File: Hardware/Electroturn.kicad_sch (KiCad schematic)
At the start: 29 parts, among them J1 Encoder Terminal, J2 Stepper Motor Terminal, SW1 Feed Switch, SW2 Motor Braking Switch, SW3 Mode Right Scroll, SW4 Mode Left Scroll, SW5 Function Btn 1, SW6 Function Btn 2, SW7 Function Btn 2, SW8 Control Panel Encoder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

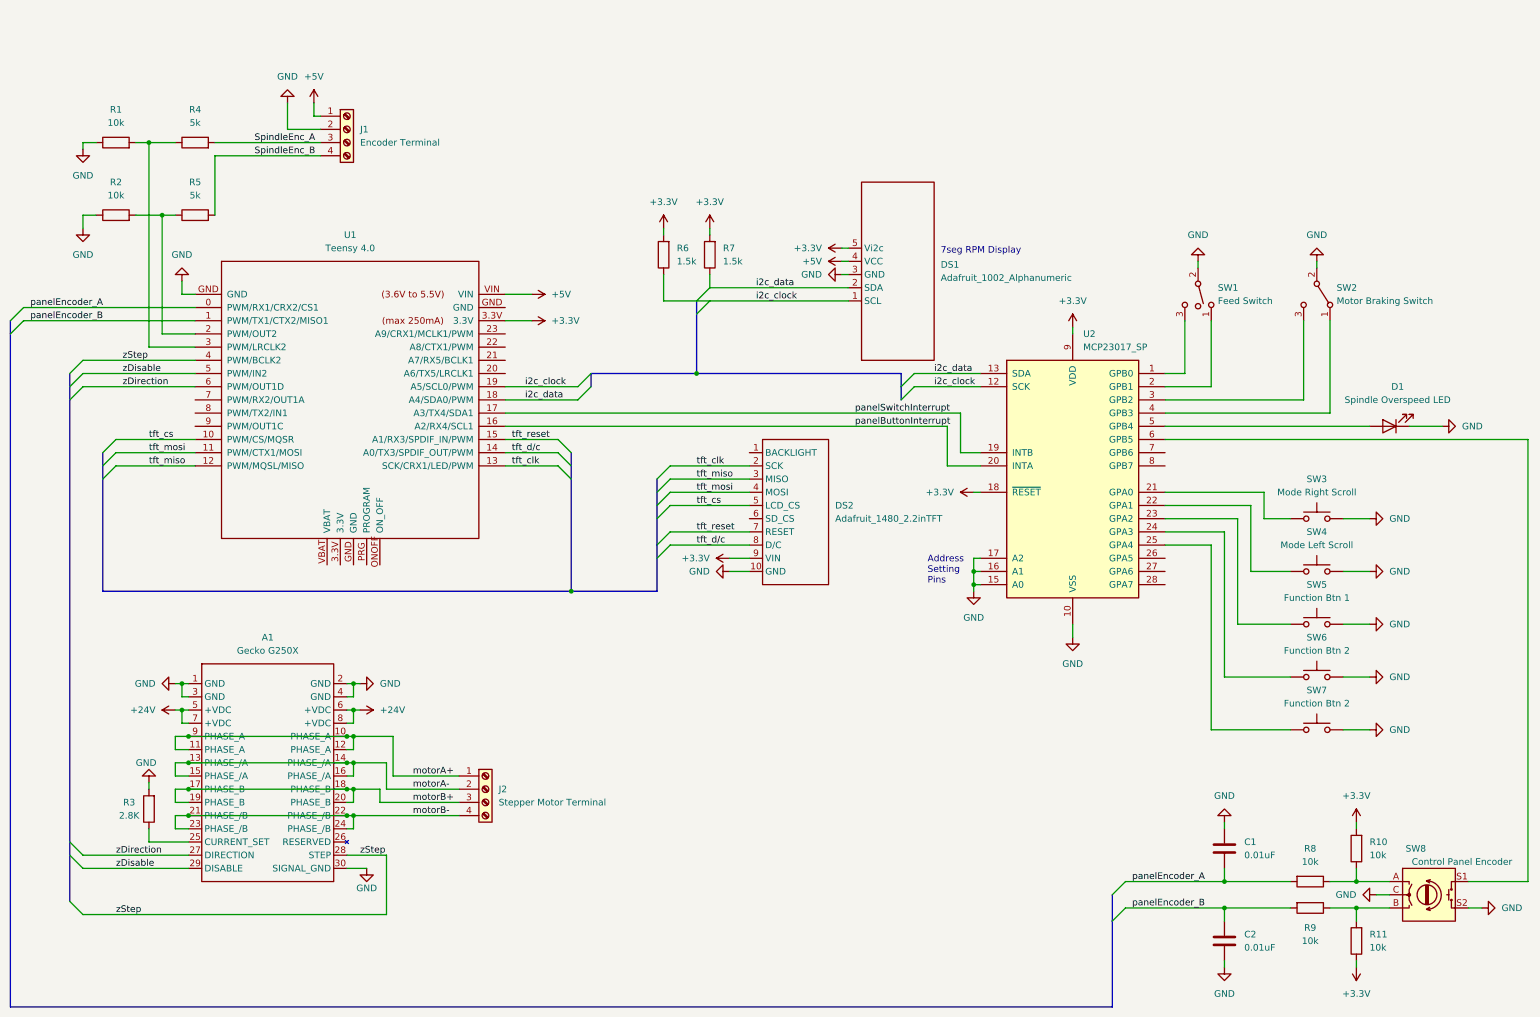
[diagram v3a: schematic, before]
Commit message: Revert "Initial PCB work" to prevent KiCad merge hell
This reverts commit 830c4b3218d3f5d7a4b251521e18afe8c7a9bcf8.
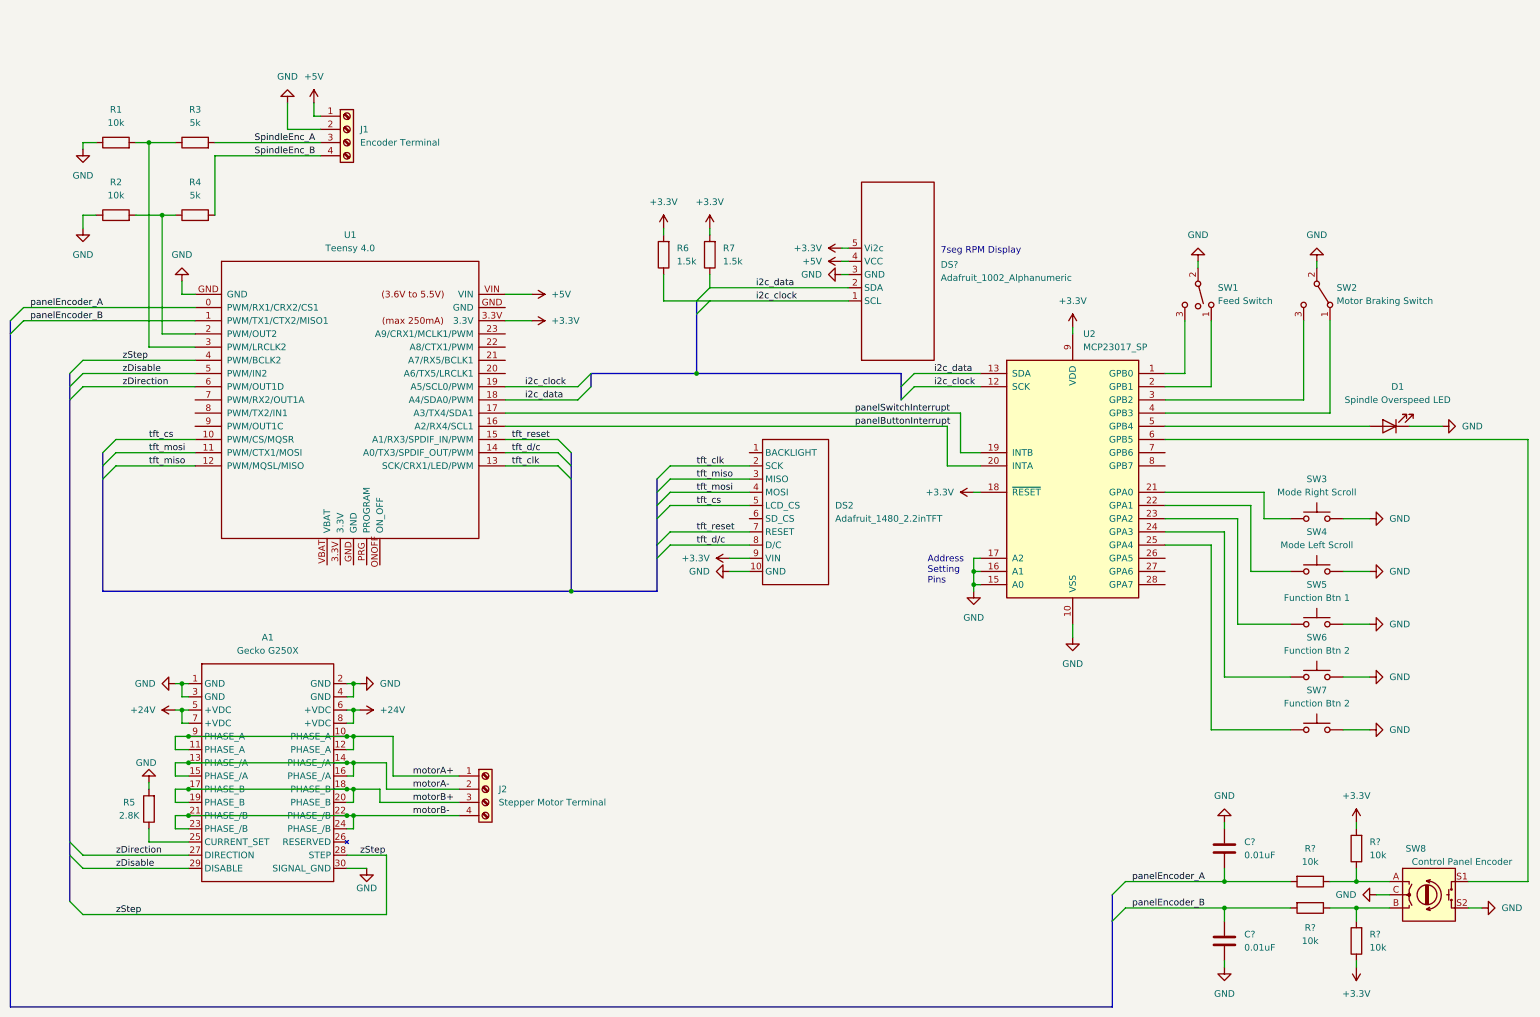
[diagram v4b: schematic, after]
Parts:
- C?: renamed from C1; footprint Capacitor_THT:C_Disc_D9.0mm_W5.0mm_P7.50mm -> (none)
- C?: renamed from C2; footprint Capacitor_THT:C_Disc_D9.0mm_W5.0mm_P7.50mm -> (none)
- D1: footprint LED_THT:LED_D5.0mm -> (none)
- DS2: footprint Electroturn_Parts:Adafruit1480_TFTwithHeaders -> (none)
- DS?: renamed from DS1; footprint Electroturn_Parts:Adafruit1002_0.54inAlphanumericBackpack -> (none)
- R6, R7: footprint Resistor_THT:R_Axial_DIN0411_L9.9mm_D3.6mm_P12.70mm_Horizontal -> (none)
- R?: renamed from R8; footprint Resistor_THT:R_Axial_DIN0411_L9.9mm_D3.6mm_P12.70mm_Horizontal -> (none)
- R?: renamed from R9; footprint Resistor_THT:R_Axial_DIN0411_L9.9mm_D3.6mm_P12.70mm_Horizontal -> (none)
- R?: renamed from R11; footprint Resistor_THT:R_Axial_DIN0411_L9.9mm_D3.6mm_P12.70mm_Horizontal -> (none)
- R?: renamed from R10; footprint Resistor_THT:R_Axial_DIN0411_L9.9mm_D3.6mm_P12.70mm_Horizontal -> (none)
- SW1: footprint Electroturn_Parts:SPDT_OnOffOn_ToggleSwitch_fromECEdepartment_CircularPads -> (none)
- SW2: footprint Electroturn_Parts:SW_SPDT_CK_ A11405RNZQ -> (none)
- SW3, SW4, SW5, SW6, SW7: footprint Button_Switch_THT:SW_PUSH_6mm -> (none)
- SW8: footprint Electroturn_Parts:CUIDevices_ACZ11BR1E20FD112C -> (none)
- renumbered R4 to R3, R5 to R4, R3 to R5

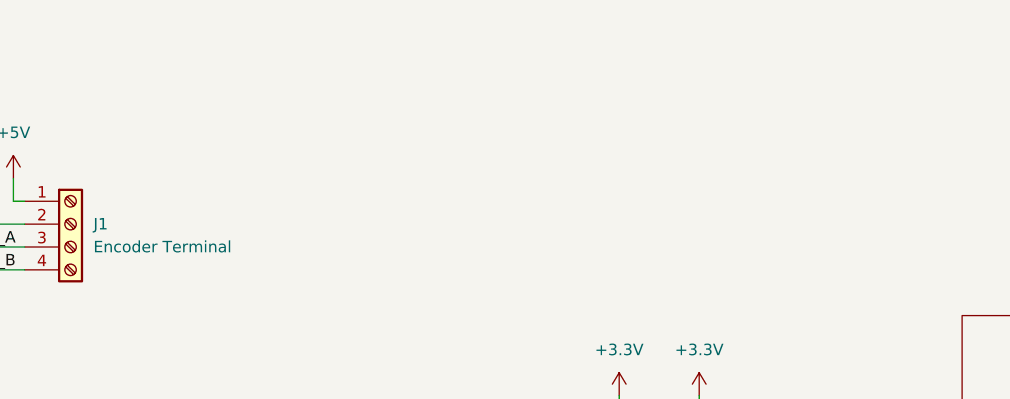
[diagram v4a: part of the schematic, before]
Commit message: Adding 5V regulator to schematic
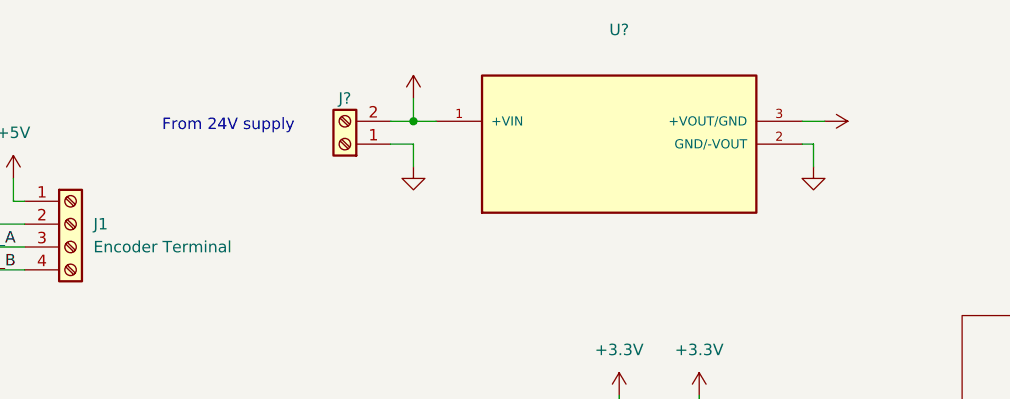
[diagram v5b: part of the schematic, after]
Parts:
- added J?: (no value), symbol Connector:Screw_Terminal_01x02
- added U?: (no value), symbol Electroturn_Parts:5vSwitchingRegulator_VXO7805-1000
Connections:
- net +24V: now also J?.2 (Pin_2), U?.1 (+VIN)
- net +5V: now also U?.3 (+VOUT/GND)
- net GND: now also J?.1 (Pin_1), U?.2 (GND/-VOUT)
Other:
- note added: "From 24V supply"
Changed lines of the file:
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@@
   (junction (at 285.75 186.69) (diameter 0) (color 0 0 0 0)
   )
+  (junction (at 154.94 30.48) (diameter 0) (color 0 0 0 0)
+  )
   (junction (at 118.11 168.91) (diameter 0) (color 0 0 0 0)
   )
@@
     (stroke (width 0) (type default) (color 0 0 0 0))
   )
+  (wire (pts (xy 199.39 33.02) (xy 199.39 35.56))
+    (stroke (width 0) (type default) (color 0 0 0 0))
+  )
   (wire (pts (xy 118.11 163.83) (xy 124.46 163.83))
     (stroke (width 0) (type default) (color 0 0 0 0))
@@
     (stroke (width 0) (type default) (color 0 0 0 0))
   )
+  (wire (pts (xy 152.4 30.48) (xy 154.94 30.48))
+    (stroke (width 0) (type default) (color 0 0 0 0))
+  )
   (wire (pts (xy 283.21 91.44) (xy 283.21 78.74))
     (stroke (width 0) (type default) (color 0 0 0 0))
@@
     (stroke (width 0) (type default) (color 0 0 0 0))
   )
+  (wire (pts (xy 198.12 30.48) (xy 200.66 30.48))
+    (stroke (width 0) (type default) (color 0 0 0 0))
+  )
   (wire (pts (xy 306.07 78.74) (xy 306.07 96.52))
     (stroke (width 0) (type default) (color 0 0 0 0))
@@
     (stroke (width 0) (type default) (color 0 0 0 0))
   )
+  (wire (pts (xy 152.4 33.02) (xy 154.94 33.02))
+    (stroke (width 0) (type default) (color 0 0 0 0))
+  )
   (wire (pts (xy 190.5 127) (xy 194.31 127))
     (stroke (width 0) (type default) (color 0 0 0 0))
@@
     (stroke (width 0) (type default) (color 0 0 0 0))
   )
+  (wire (pts (xy 154.94 30.48) (xy 154.94 27.94))
+    (stroke (width 0) (type default) (color 0 0 0 0))
+  )
   (wire (pts (xy 124.46 168.91) (xy 138.43 168.91))
     (stroke (width 0) (type default) (color 0 0 0 0))
@@
     (stroke (width 0) (type default) (color 0 0 0 0))
   )
+  (wire (pts (xy 154.94 33.02) (xy 154.94 35.56))
+    (stroke (width 0) (type default) (color 0 0 0 0))
+  )
   (bus (pts (xy 160.02 130.81) (xy 176.53 130.81))
     (stroke (width 0) (type default) (color 0 0 0 0))
@@
     (stroke (width 0) (type default) (color 0 0 0 0))
   )
+  (wire (pts (xy 154.94 30.48) (xy 157.48 30.48))
+    (stroke (width 0) (type default) (color 0 0 0 0))
+  )
   (wire (pts (xy 91.44 44.45) (xy 111.76 44.45))
     (stroke (width 0) (type default) (color 0 0 0 0))
@@
     (stroke (width 0) (type default) (color 0 0 0 0))
   )
+  (wire (pts (xy 198.12 33.02) (xy 199.39 33.02))
+    (stroke (width 0) (type default) (color 0 0 0 0))
+  )
   (wire (pts (xy 184.15 74.93) (xy 186.69 74.93))
     (stroke (width 0) (type default) (color 0 0 0 0))
@@
   )
   (text "7seg RPM Display" (at 231.14 66.04 0)
+    (effects (font (size 1.27 1.27)) (justify left bottom))
+  )
+  (text "From 24V supply" (at 127 31.75 0)
     (effects (font (size 1.27 1.27)) (justify left bottom))
   )
@@
     )
     (property "Datasheet" "~" (id 3) (at 87.63 58.42 0)
+      (effects (font (size 1.27 1.27)) hide)
+    )
+    (pin "1")
+    (pin "2")
+  )
+  (symbol (lib_id "Connector:Screw_Terminal_01x02") (at 147.32 33.02 180) (unit 1)
+    (in_bom yes) (on_board yes)
+    (property "Reference" "J?" (id 0) (at 147.32 27.94 0))
+    (property "Value" "" (id 1) (at 137.16 25.4 0))
+    (property "Footprint" "" (id 2) (at 147.32 33.02 0)
+      (effects (font (size 1.27 1.27)) hide)
+    )
+    (property "Datasheet" "~" (id 3) (at 147.32 33.02 0)
       (effects (font (size 1.27 1.27)) hide)
     )
@@
     (pin "2")
   )
+  (symbol (lib_id "Electroturn_Parts:5vSwitchingRegulator_VXO7805-1000") (at 177.8 33.02 0) (unit 1)
+    (in_bom yes) (on_board yes) (fields_autoplaced)
+    (property "Reference" "U?" (id 0) (at 177.8 20.32 0))
+    (property "Value" "" (id 1) (at 177.8 22.86 0))
+    (property "Footprint" "" (id 2) (at 162.56 52.07 0)
+      (effects (font (size 1.27 1.27)) (justify left bottom) hide)
+    )
+    (property "Datasheet" "" (id 3) (at 177.8 33.02 0)
+      (effects (font (size 1.27 1.27)) (justify left bottom) hide)
+    )
+    (property "MANUFACTURER" "CUI INC" (id 4) (at 162.56 54.61 0)
+      (effects (font (size 1.27 1.27)) (justify left bottom) hide)
+    )
+    (property "STANDARD" "MANUFACTURER RECOMMENDATIONS" (id 5) (at 162.56 46.99 0)
+      (effects (font (size 1.27 1.27)) (justify left bottom) hide)
+    )
+    (property "PARTREV" "1.0" (id 6) (at 162.56 49.53 0)
+      (effects (font (size 1.27 1.27)) (justify left bottom) hide)
+    )
+    (pin "1")
+    (pin "2")
+    (pin "3")
+  )
   (symbol (lib_id "power:GND") (at 314.96 189.23 270) (unit 1)
     (in_bom yes) (on_board yes) (fields_autoplaced)
@@
     (pin "5")
   )
+  (symbol (lib_id "power:+24V") (at 154.94 27.94 0) (unit 1)
+    (in_bom yes) (on_board yes) (fields_autoplaced)
+    (property "Reference" "#PWR?" (id 0) (at 154.94 31.75 0)
+      (effects (font (size 1.27 1.27)) hide)
+    )
+    (property "Value" "" (id 1) (at 154.94 22.86 0))
+    (property "Footprint" "" (id 2) (at 154.94 27.94 0)
+      (effects (font (size 1.27 1.27)) hide)
+    )
+    (property "Datasheet" "" (id 3) (at 154.94 27.94 0)
+      (effects (font (size 1.27 1.27)) hide)
+    )
+    (pin "1")
+  )
   (symbol (lib_id "power:GND") (at 85.09 71.12 180) (unit 1)
     (in_bom yes) (on_board yes) (fields_autoplaced)
@@
     (pin "1")
   )
+  (symbol (lib_id "power:+5V") (at 200.66 30.48 270) (unit 1)
+    (in_bom yes) (on_board yes) (fields_autoplaced)
+    (property "Reference" "#PWR?" (id 0) (at 196.85 30.48 0)
+      (effects (font (size 1.27 1.27)) hide)
+    )
+    (property "Value" "" (id 1) (at 204.47 30.4799 90)
+      (effects (font (size 1.27 1.27)) (justify left))
+    )
+    (property "Footprint" "" (id 2) (at 200.66 30.48 0)
+      (effects (font (size 1.27 1.27)) hide)
+    )
+    (property "Datasheet" "" (id 3) (at 200.66 30.48 0)
+      (effects (font (size 1.27 1.27)) hide)
+    )
+    (pin "1")
+  )
   (symbol (lib_id "Device:R") (at 72.39 58.42 90) (unit 1)
     (in_bom yes) (on_board yes) (fields_autoplaced)
@@
     (pin "1")
   )
+  (symbol (lib_id "power:GND") (at 199.39 35.56 0) (unit 1)
+    (in_bom yes) (on_board yes) (fields_autoplaced)
+    (property "Reference" "#PWR?" (id 0) (at 199.39 41.91 0)
+      (effects (font (size 1.27 1.27)) hide)
+    )
+    (property "Value" "" (id 1) (at 199.39 40.64 0))
+    (property "Footprint" "" (id 2) (at 199.39 35.56 0)
+      (effects (font (size 1.27 1.27)) hide)
+    )
+    (property "Datasheet" "" (id 3) (at 199.39 35.56 0)
+      (effects (font (size 1.27 1.27)) hide)
+    )
+    (pin "1")
+  )
+  (symbol (lib_id "power:GND") (at 154.94 35.56 0) (unit 1)
+    (in_bom yes) (on_board yes) (fields_autoplaced)
+    (property "Reference" "#PWR?" (id 0) (at 154.94 41.91 0)
+      (effects (font (size 1.27 1.27)) hide)
+    )
+    (property "Value" "" (id 1) (at 154.94 40.64 0))
+    (property "Footprint" "" (id 2) (at 154.94 35.56 0)
+      (effects (font (size 1.27 1.27)) hide)
+    )
+    (property "Datasheet" "" (id 3) (at 154.94 35.56 0)
+      (effects (font (size 1.27 1.27)) hide)
+    )
+    (pin "1")
+  )
   (symbol (lib_id "Device:R") (at 177.8 66.04 180) (unit 1)
     (in_bom yes) (on_board yes) (fields_autoplaced)
@@
       (reference "#PWR?") (unit 1) (value "+3.3V") (footprint "")
     )
+    (path "/a3ff6a1a-e884-47cd-bb45-c1f2c3629911"
+      (reference "#PWR?") (unit 1) (value "+24V") (footprint "")
+    )
+    (path "/c658a1aa-b428-47f8-a9f0-5d75e55e4300"
+      (reference "#PWR?") (unit 1) (value "+5V") (footprint "")
+    )
     (path "/ca7b197f-7808-47de-a461-95f69fe0e8ed"
       (reference "#PWR?") (unit 1) (value "+3.3V") (footprint "")
     )
+    (path "/cfce671f-e48e-4e63-a629-54c42fbd2282"
+      (reference "#PWR?") (unit 1) (value "GND") (footprint "")
+    )
+    (path "/d3863af8-ddbd-48dd-961e-13bfab033632"
+      (reference "#PWR?") (unit 1) (value "GND") (footprint "")
+    )
     (path "/fc84a68c-83b8-4be3-a49a-01e55462a4b3"
       (reference "#PWR?") (unit 1) (value "GND") (footprint "")
@@
       (reference "J2") (unit 1) (value "Stepper Motor Terminal") (footprint "Electroturn_Parts:ScrewTerminal4_OSTVN04A150")
     )
+    (path "/411c8e4d-e251-45bc-9aa2-3247cf5e06b8"
+      (reference "J?") (unit 1) (value "Screw_Terminal_01x02") (footprint "")
+    )
     (path "/589ddb03-c8eb-44fe-8345-f248307d14f2"
       (reference "R1") (unit 1) (value "10k") (footprint "Resistor_THT:R_Axial_DIN0411_L9.9mm_D3.6mm_P12.70mm_Horizontal")
@@
       (reference "U2") (unit 1) (value "MCP23017_SP") (footprint "Package_DIP:DIP-28_W7.62mm")
     )
-  )
+    (path "/6cf4313f-0a5b-4b3c-a6dd-63728dcdf74d"
+      (reference "U?") (unit 1) (value "5vSwitchingRegulator_VXO7805-1000") (footprint "CONV_VXO7805-1000")
+    )
+  )
